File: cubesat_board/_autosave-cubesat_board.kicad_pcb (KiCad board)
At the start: 2 copper layers, 91.4 x 91.4 mm, 3 parts, among them J1 CONN_02X26, J2 CONN_02X26

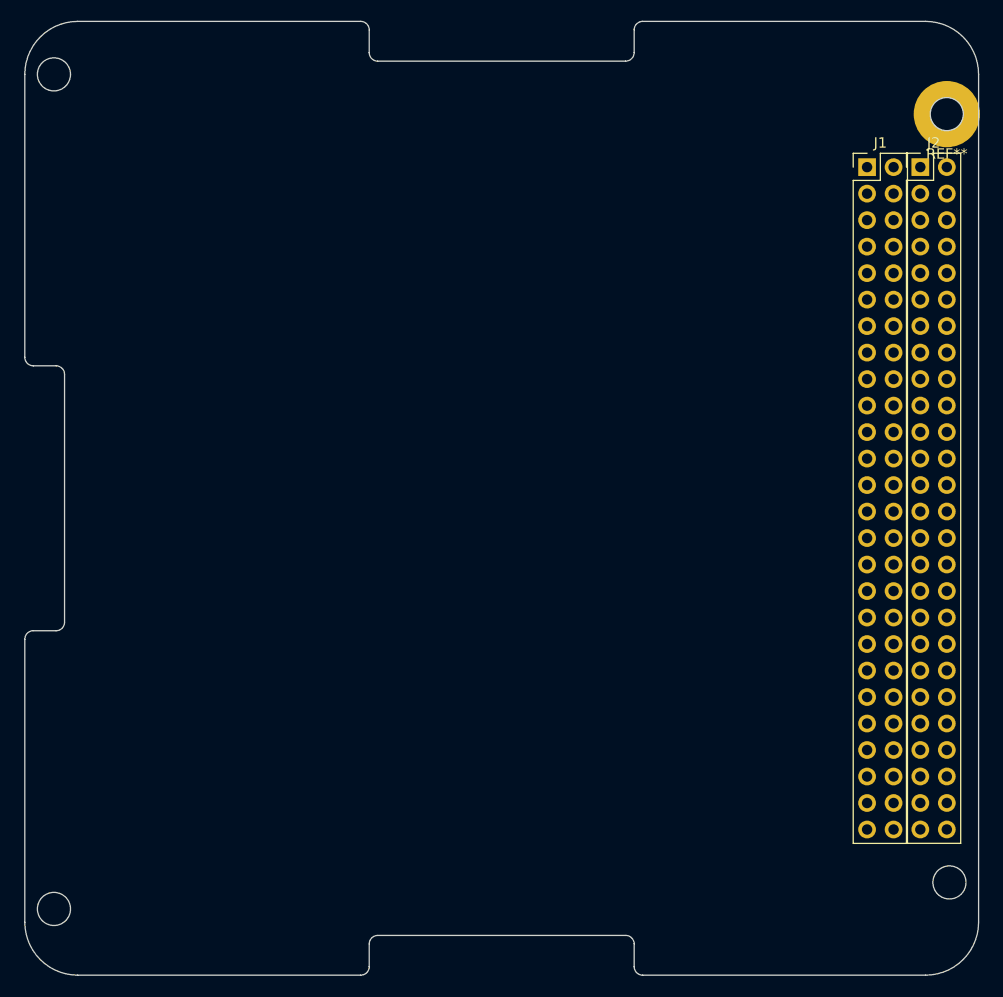
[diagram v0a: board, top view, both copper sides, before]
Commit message: Defined cubesat board to be 3.6" a side.
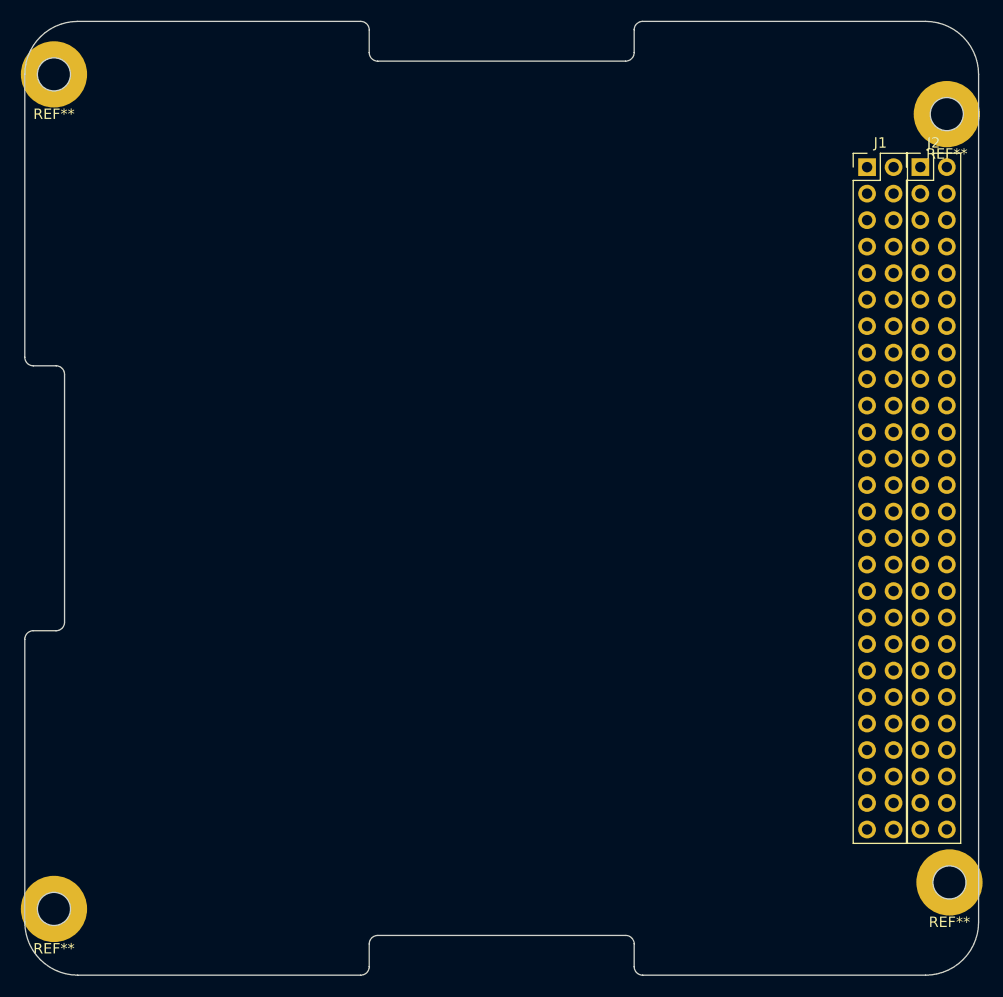
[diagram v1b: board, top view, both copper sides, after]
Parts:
- added REF**: 0.125in mounting hole, mounting_holes:0.125in_mounting_hole, F.Cu at (102.8, 96.9)
- added REF**: 0.125in mounting hole, mounting_holes:0.125in_mounting_hole, F.Cu at (16.9, 99.4)
- added REF**: 0.125in mounting hole, mounting_holes:0.125in_mounting_hole, F.Cu at (16.9, 19.4)
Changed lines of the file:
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@@
     (links 0)
     (no_connects 0)
-    (area 12.053099 11.989599 265.698334 103.529601)
+    (area 14.085099 14.275599 106.293094 105.815601)
     (thickness 1.6)
     (drawings 36)
     (tracks 0)
     (zones 0)
-    (modules 3)
+    (modules 6)
     (nets 105)
   )
@@
     (fp_text reference REF** (at 0 3.81) (layer F.SilkS)
       (effects (font (size 1 1) (thickness 0.15)))
+    )
+    (fp_text value "0.125in mounting hole" (at 0 -2.54) (layer F.Fab)
+      (effects (font (size 0.254 0.254) (thickness 0.0508)))
+    )
+    (pad "" np_thru_hole circle (at 0 0) (size 6.35 6.35) (drill 3.175) (layers *.Cu *.Mask))
+  )
+  (module mounting_holes:0.125in_mounting_hole (layer F.Cu)
+    (at 102.78376 96.87572)
+    (fp_text reference REF** (at 0 3.81) (layer F.SilkS)
+      (effects (font (size 1 1) (thickness 0.15)))
+    )
+    (fp_text value "0.125in mounting hole" (at 0 -2.54) (layer F.Fab)
+      (effects (font (size 0.254 0.254) (thickness 0.0508)))
+    )
+    (pad "" np_thru_hole circle (at 0 0) (size 6.35 6.35) (drill 3.175) (layers *.Cu *.Mask))
+  )
+  (module mounting_holes:0.125in_mounting_hole (layer F.Cu)
+    (at 16.93176 99.41572)
+    (fp_text reference REF** (at 0 3.81) (layer F.SilkS)
+      (effects (font (size 1 1) (thickness 0.15)))
+    )
+    (fp_text value "0.125in mounting hole" (at 0 -2.54) (layer F.Fab)
+      (effects (font (size 0.254 0.254) (thickness 0.0508)))
+    )
+    (pad "" np_thru_hole circle (at 0 0) (size 6.35 6.35) (drill 3.175) (layers *.Cu *.Mask))
+  )
+  (module mounting_holes:0.125in_mounting_hole (layer F.Cu)
+    (at 16.93176 19.40572)
+    (fp_text reference REF** (at 0 3.81) (layer F.SilkS)
+      (effects (font (size 1 1) (thickness 0.15)))
